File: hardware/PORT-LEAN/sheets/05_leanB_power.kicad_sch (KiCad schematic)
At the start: 155 parts, among them K701 HFE82V-300C/1000-24-H-C5-1, K702 G7L-2A-X DC24, Q701 PMV30ENEAR, Q702 BSS138BK, Q703 IRFR9214TRPbF, Q704 BSS138BK, Q705 IRFR9214TRPbF, Q801 BSS138BK, Q802 BSS138BK, U501 CNY65B, U601 OPA2388IDR, U602 TLV3502AIDCNR, U603 SN74LVC1G32DBVR, U604 TLV3502AIDCNR, U605 SN74LVC1G32DBVR, U606 OPA2388IDR, U607 OPA2388IDR, U608 TLV3502AIDCNR, U609 TLV3502AIDCNR, U610 SN74LVC1G11DBVR, U701 SN74LVC1G11DBVR, U702 SN74LVC1G11DBVR, U703 SN74LVC1G32DBVR, U704 SN74LVC1G11DBVR, U801 OPA2388IDR, U802 CA-IS3417WT, U803 CA-IS3417WT, X501 006710340, X502 006710340, X503 006710340, X504 006710340

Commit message: Board revisions PV-PWR A2 / PV-CTL A1, inverter filter magnetics, documentation refresh (D-056..D-058)
Boards (every build check passes)
- PV-PWR / PV-PWR-4 rev A2: seventh battery-side film capacitor on the three-phase board (closes the
  load-rejection overshoot), bleeder 8 x 73.2 k so the bank still discharges within its 10-minute label.
- PV-CTL rev A1: hardware over-current window 68.9-79.9 A, thresholds derived from each sensor's own
  reference; the board-to-board contract carries the four references on the former 24 V / 5 V pins.
- Records aligned (contract comments, architecture corrections, port-current bandwidth); the frozen
  platform's module BOMs are kept instead of being re-rolled from the cost-first thermal data.

Magnetics
- Inverter filter designed and verified: L1, L2 and the AC common-mode choke (design_pcs_*.json). The filter
  comes to 745 USD at catalogue prices and 611 USD at 5,000 units, against 207 / 167 in the study: the
  inverter's cost is provisional and its stage and filter are being re-optimised.
- PV inductor loss check made non-circular; hot-spot margin reported per build (PV-P100/110: -5.3 K, MG-17).

Results: PV-P75 952 USD at catalogue prices / 796 USD at 5,000 units; Megarevo comparison 2 better,
24 meet, 3 below, 5 not assessed. Documentation corrected for the revised boards (51 statements).
Everything is calculated or estimated; nothing is bench-validated.

Co-Authored-By: Claude Fable 5.1 <noreply@anthropic.com>
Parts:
- R710, R711, R712, R713, R714, R715, R716, R717: value 82.5k -> 73.2k
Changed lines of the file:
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@@
 			)
 		)
-		(property "Value" "82.5k"
+		(property "Value" "73.2k"
 			(at 655.32 274.196 90)
 			(show_name no)
@@
 			)
 		)
-		(property "Description" "Resistor 82.5k 1% 1210 HV thick film, >= 200 V working"
+		(property "Description" "Resistor 73.2k 1% 1210 HV thick film, >= 200 V working"
 			(at 655.32 271.78 0)
 			(hide yes)
@@
 			)
 		)
-		(property "Value" "82.5k"
+		(property "Value" "73.2k"
 			(at 627.38 274.196 90)
 			(show_name no)
@@
 			)
 		)
-		(property "Description" "Resistor 82.5k 1% 1210 HV thick film, >= 200 V working"
+		(property "Description" "Resistor 73.2k 1% 1210 HV thick film, >= 200 V working"
 			(at 627.38 271.78 0)
 			(hide yes)
@@
 			)
 		)
-		(property "Value" "82.5k"
+		(property "Value" "73.2k"
 			(at 708.66 274.196 90)
 			(show_name no)
@@
 			)
 		)
-		(property "Description" "Resistor 82.5k 1% 1210 HV thick film, >= 200 V working"
+		(property "Description" "Resistor 73.2k 1% 1210 HV thick film, >= 200 V working"
 			(at 708.66 271.78 0)
 			(hide yes)
@@
 			)
 		)
-		(property "Value" "82.5k"
+		(property "Value" "73.2k"
 			(at 680.72 274.196 90)
 			(show_name no)
@@
 			)
 		)
-		(property "Description" "Resistor 82.5k 1% 1210 HV thick film, >= 200 V working"
+		(property "Description" "Resistor 73.2k 1% 1210 HV thick film, >= 200 V working"
 			(at 680.72 271.78 0)
 			(hide yes)
@@
 			)
 		)
-		(property "Value" "82.5k"
+		(property "Value" "73.2k"
 			(at 599.44 274.196 90)
 			(show_name no)
@@
 			)
 		)
-		(property "Description" "Resistor 82.5k 1% 1210 HV thick film, >= 200 V working"
+		(property "Description" "Resistor 73.2k 1% 1210 HV thick film, >= 200 V working"
 			(at 599.44 271.78 0)
 			(hide yes)
@@
 			)
 		)
-		(property "Value" "82.5k"
+		(property "Value" "73.2k"
 			(at 571.5 274.196 90)
 			(show_name no)
@@
 			)
 		)
-		(property "Description" "Resistor 82.5k 1% 1210 HV thick film, >= 200 V working"
+		(property "Description" "Resistor 73.2k 1% 1210 HV thick film, >= 200 V working"
 			(at 571.5 271.78 0)
 			(hide yes)
@@
 			)
 		)
-		(property "Value" "82.5k"
+		(property "Value" "73.2k"
 			(at 764.54 274.196 90)
 			(show_name no)
@@
 			)
 		)
-		(property "Description" "Resistor 82.5k 1% 1210 HV thick film, >= 200 V working"
+		(property "Description" "Resistor 73.2k 1% 1210 HV thick film, >= 200 V working"
 			(at 764.54 271.78 0)
 			(hide yes)
@@
 			)
 		)
-		(property "Value" "82.5k"
+		(property "Value" "73.2k"
 			(at 736.6 274.196 90)
 			(show_name no)
@@
 			)
 		)
-		(property "Description" "Resistor 82.5k 1% 1210 HV thick film, >= 200 V working"
+		(property "Description" "Resistor 73.2k 1% 1210 HV thick film, >= 200 V working"
 			(at 736.6 271.78 0)
 			(hide yes)

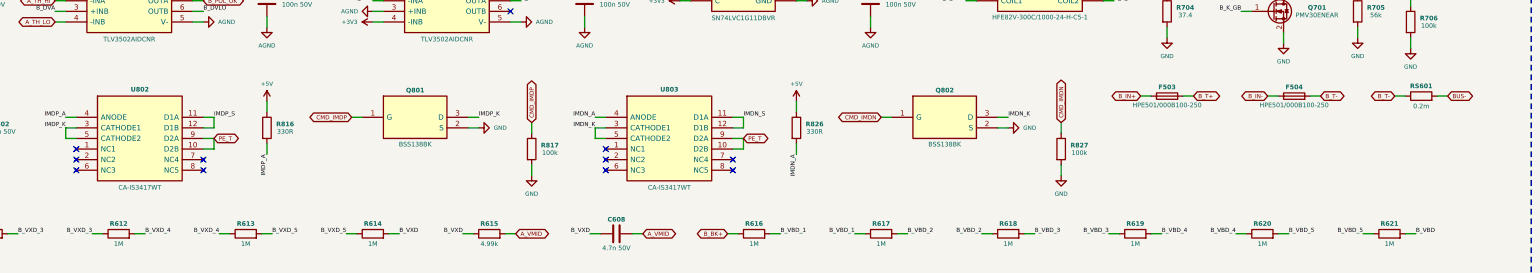
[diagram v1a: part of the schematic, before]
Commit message: Resolve the independent PCM review of 033d8d8 (PCM-01..27): verify, classify, fix at the root (D-065..D-072)
Register gen/data/review_pcm.csv: 27 findings, each verified before a change - 21 Confirmed, 2 Firmware
Handled, 3 Improvement Recommended, 1 Not Applicable; 20 closed, 7 open with their closing path.

PV family (D-065, D-072): the 45 A port rating no longer clamps the inductor current in the near-unity
band (inductor rating 47.7 A there; 550/550 V 73.3 kW; rated power from 562 V); control model re-based on
the drawn boards with a published delivered-power envelope per product and direction; leg commutation
re-run on the drawn Jianghai capacitors (1374 V worst vs 1445 V); comparator common-mode term in every
trip band (window 67.9-80.5 A, the 1.10 margin rule missed by 0.58 A and left open; firmware OV derived
from the drawn band, 1034 V); one fan-supply contract; cold-start passive-power restriction modelled;
port A interface declared; aux pull-in and retry rules.

PCS-P125 (D-066, D-067): control study sim/pcs_control.py (PR current loop 1750 Hz, PM >= 48.7 deg to
SCR 5 with the passive damping branch, PLL, DC-link loop, grid forming, state machine); DC-link inventory
409.4 uF with bleeders, precharge rating and the 15 min label re-derived; upper-half limit in firmware;
P-Q-Vdc-Vac envelope (AC-02's 600 V full-load figure not reachable at a +15 % grid: owner's decision);
R_DS(on) acceptance rule for the six paralleled devices; DESAT string 3 -> 2 diodes (band 6.41-9.37 V);
fuse-contactor coordination bands and installation requirements; phase-current sensor frozen to Sinomags
STK-250HO/4 and the control-board ladders re-valued; Al2O3 pad text.

DAB-D60 (D-068): study vs drawn-board identity made explicit; short-circuit chain corrected (energy-
equivalent 0.99 x the assumed withstand; release block t_SC >= 2.22 us / E_SC >= 2.18 J); admitted map
follows the 1200 V deck envelope (900-950 V rows derated until a double-pulse test); zero/light-load policy;
0.41 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
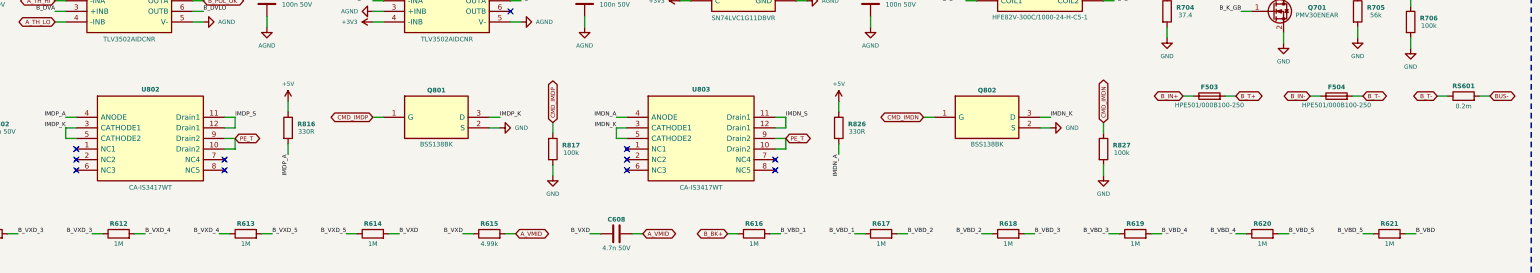
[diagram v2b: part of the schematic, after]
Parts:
- D702, D704: Manufacturer Bourns -> MDD (Microdiode Semiconductor)
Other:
- moved on the sheet: F503, F504, Q801, Q802, R816, R817, R826, R827, RS601, U802, U803
